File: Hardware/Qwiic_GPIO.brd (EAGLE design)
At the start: 38.1 x 38.1 mm, 65 parts, among them J2 SMD, J3 PTH, J4 SMD, U3 TCA9534U

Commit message: Panel/production files
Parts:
- moved U$33 1.65 mm to (5.21, 5.46)
- moved U$34 1.65 mm to (3.56, 5.46)
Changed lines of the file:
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@@
 <layer number="23" name="tOrigins" color="15" fill="1" visible="yes" active="yes"/>
 <layer number="24" name="bOrigins" color="15" fill="1" visible="yes" active="yes"/>
-<layer number="25" name="tNames" color="7" fill="1" visible="no" active="yes"/>
-<layer number="26" name="bNames" color="7" fill="1" visible="no" active="yes"/>
-<layer number="27" name="tValues" color="7" fill="1" visible="no" active="yes"/>
-<layer number="28" name="bValues" color="7" fill="1" visible="no" active="yes"/>
-<layer number="29" name="tStop" color="7" fill="3" visible="no" active="yes"/>
-<layer number="30" name="bStop" color="7" fill="6" visible="no" active="yes"/>
-<layer number="31" name="tCream" color="7" fill="4" visible="no" active="yes"/>
-<layer number="32" name="bCream" color="7" fill="5" visible="no" active="yes"/>
-<layer number="33" name="tFinish" color="6" fill="3" visible="no" active="yes"/>
-<layer number="34" name="bFinish" color="6" fill="6" visible="no" active="yes"/>
-<layer number="35" name="tGlue" color="7" fill="4" visible="no" active="yes"/>
-<layer number="36" name="bGlue" color="7" fill="5" visible="no" active="yes"/>
-<layer number="37" name="tTest" color="7" fill="1" visible="no" active="yes"/>
-<layer number="38" name="bTest" color="7" fill="1" visible="no" active="yes"/>
-<layer number="39" name="tKeepout" color="4" fill="11" visible="no" active="yes"/>
-<layer number="40" name="bKeepout" color="1" fill="11" visible="no" active="yes"/>
-<layer number="41" name="tRestrict" color="4" fill="10" visible="no" active="yes"/>
-<layer number="42" name="bRestrict" color="1" fill="10" visible="no" active="yes"/>
-<layer number="43" name="vRestrict" color="2" fill="10" visible="no" active="yes"/>
-<layer number="44" name="Drills" color="7" fill="1" visible="no" active="yes"/>
+<layer number="25" name="tNames" color="7" fill="1" visible="yes" active="yes"/>
+<layer number="26" name="bNames" color="7" fill="1" visible="yes" active="yes"/>
+<layer number="27" name="tValues" color="7" fill="1" visible="yes" active="yes"/>
+<layer number="28" name="bValues" color="7" fill="1" visible="yes" active="yes"/>
+<layer number="29" name="tStop" color="7" fill="3" visible="yes" active="yes"/>
+<layer number="30" name="bStop" color="7" fill="6" visible="yes" active="yes"/>
+<layer number="31" name="tCream" color="7" fill="4" visible="yes" active="yes"/>
+<layer number="32" name="bCream" color="7" fill="5" visible="yes" active="yes"/>
+<layer number="33" name="tFinish" color="6" fill="3" visible="yes" active="yes"/>
+<layer number="34" name="bFinish" color="6" fill="6" visible="yes" active="yes"/>
+<layer number="35" name="tGlue" color="7" fill="4" visible="yes" active="yes"/>
+<layer number="36" name="bGlue" color="7" fill="5" visible="yes" active="yes"/>
+<layer number="37" name="tTest" color="7" fill="1" visible="yes" active="yes"/>
+<layer number="38" name="bTest" color="7" fill="1" visible="yes" active="yes"/>
+<layer number="39" name="tKeepout" color="4" fill="11" visible="yes" active="yes"/>
+<layer number="40" name="bKeepout" color="1" fill="11" visible="yes" active="yes"/>
+<layer number="41" name="tRestrict" color="4" fill="10" visible="yes" active="yes"/>
+<layer number="42" name="bRestrict" color="1" fill="10" visible="yes" active="yes"/>
+<layer number="43" name="vRestrict" color="2" fill="10" visible="yes" active="yes"/>
+<layer number="44" name="Drills" color="7" fill="1" visible="yes" active="yes"/>
 <layer number="45" name="Holes" color="7" fill="1" visible="yes" active="yes"/>
-<layer number="46" name="Milling" color="3" fill="1" visible="no" active="yes"/>
-<layer number="47" name="Measures" color="7" fill="1" visible="no" active="yes"/>
-<layer number="48" name="Document" color="7" fill="1" visible="no" active="yes"/>
-<layer number="49" name="Reference" color="7" fill="1" visible="no" active="yes"/>
-<layer number="50" name="dxf" color="7" fill="1" visible="no" active="yes"/>
+<layer number="46" name="Milling" color="3" fill="1" visible="yes" active="yes"/>
+<layer number="47" name="Measures" color="7" fill="1" visible="yes" active="yes"/>
+<layer number="48" name="Document" color="7" fill="1" visible="yes" active="yes"/>
+<layer number="49" name="Reference" color="7" fill="1" visible="yes" active="yes"/>
+<layer number="50" name="dxf" color="7" fill="1" visible="yes" active="yes"/>
 <layer number="51" name="tDocu" color="6" fill="1" visible="yes" active="yes"/>
-<layer number="52" name="bDocu" color="7" fill="1" visible="no" active="yes"/>
+<layer number="52" name="bDocu" color="7" fill="1" visible="yes" active="yes"/>
 <layer number="91" name="Nets" color="2" fill="1" visible="no" active="no"/>
 <layer number="92" name="Busses" color="1" fill="1" visible="no" active="no"/>
@@
 <element name="U$37" library="buzzard_labels (5)" package="04" value="" x="3.683" y="29.845" smashed="yes" rot="R90"/>
 <element name="U$29" library="buzzard_labels (5)" package="15" value="" x="5.461" y="29.972" smashed="yes" rot="R90"/>
-<element name="U$33" library="buzzard_labels (5)" package="20" value="" x="3.556" y="5.461" smashed="yes" rot="R90"/>
-<element name="U$34" library="buzzard_labels (5)" package="31" value="" x="5.207" y="5.461" smashed="yes" rot="R90"/>
+<element name="U$33" library="buzzard_labels (5)" package="20" value="" x="5.207" y="5.461" smashed="yes" rot="R90"/>
+<element name="U$34" library="buzzard_labels (5)" package="31" value="" x="3.556" y="5.461" smashed="yes" rot="R90"/>
 <element name="U$35" library="buzzard_labels (5)" package="GND2" value="" x="1.905" y="28.829" smashed="yes" rot="R90"/>
 <element name="U$38" library="buzzard_labels (5)" package="3V33" value="" x="7.239" y="28.829" smashed="yes" rot="R90"/>

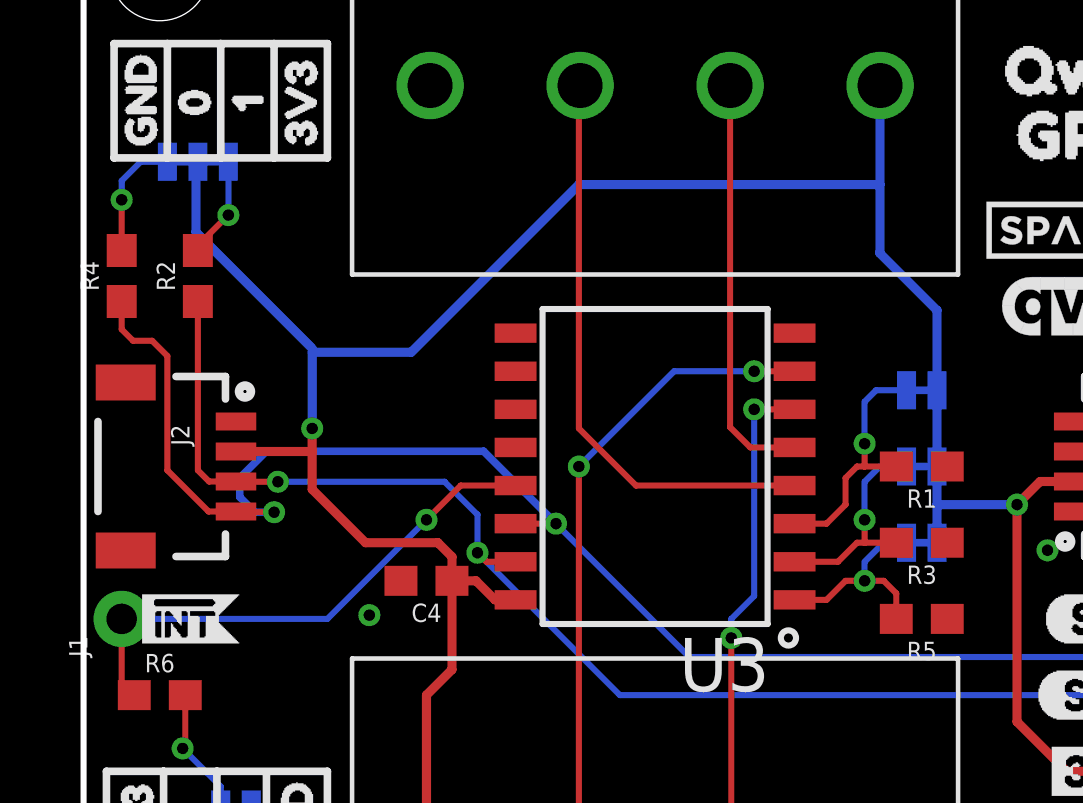
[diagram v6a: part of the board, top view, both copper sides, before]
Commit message: Added PWR LED, made labels larger
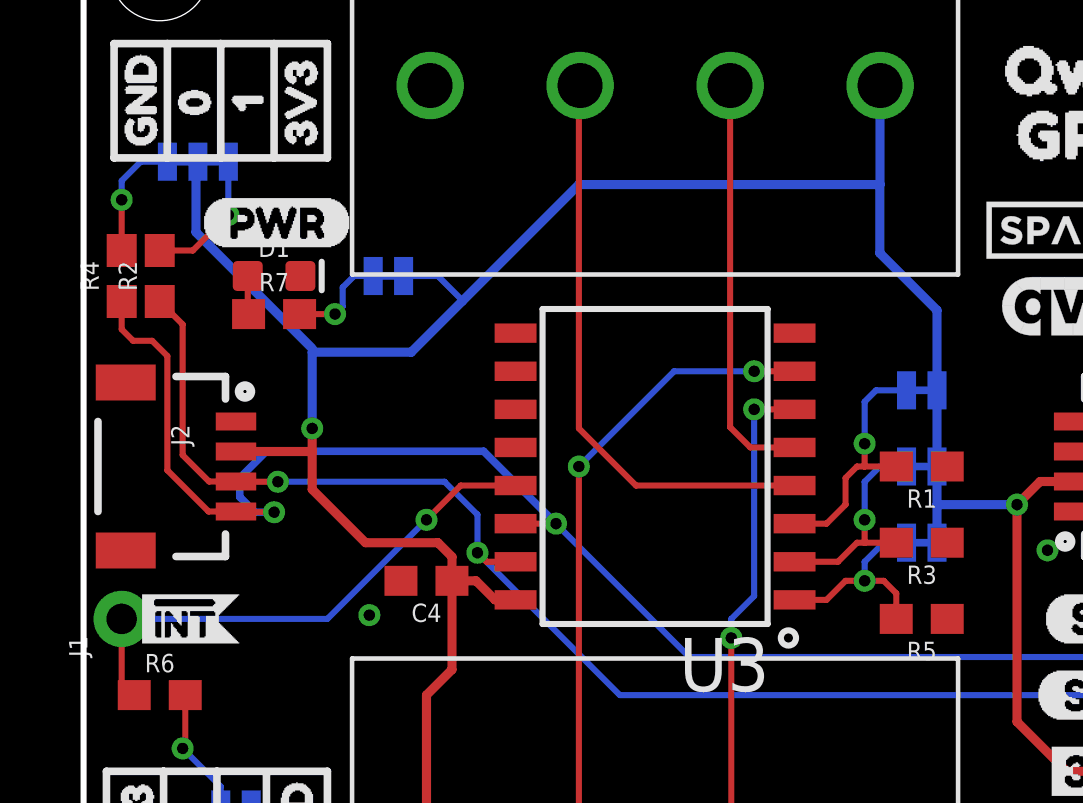
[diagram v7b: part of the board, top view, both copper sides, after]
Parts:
- removed U$14, U$15: (no value), buzzard_labels (47):__3V3__3
- removed U$16: (no value), buzzard_labels (49):_____1_____1
- removed U$17: (no value), buzzard_labels (49):______0______0
- removed U$18: (no value), buzzard_labels (48):_____3_____2
- removed U$19: (no value), buzzard_labels (48):______2______1
- removed U$4, U$6: (no value), buzzard_labels (48):__GND__0
- added 3V3: JUMPER-SMT_2_NC_TRACE_SILK, SparkFun-Jumpers:SMT-JUMPER_2_NC_TRACE_SILK
- added D1: RED, SparkFun-LED:LED-0603
- added R7: 1k, SparkFun-Resistors:0603
- added U$30, U$31: (no value), buzzard_labels (66):INT1
- added U$39, U$40: (no value), buzzard_labels (66):PWR0
- added U$41: (no value), buzzard_labels (68):____0____1
- added U$42: (no value), buzzard_labels (68):____2____3
- added U$43: (no value), buzzard_labels (68):____3____4
- added U$44: (no value), buzzard_labels (68):_____1____2
- added U$45, U$46: (no value), buzzard_labels (68):GND0
- added U$47, U$48: (no value), buzzard_labels (71):_3V3_0
- moved R2 1.27 mm to (2.54, 25.4)
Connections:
- new net N$2: D1.A, R7.1
- new net N$3: 3V3.1, R7.2
- net 3.3V: now also 3V3.2
- net GND: now also D1.C
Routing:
- net N$3: track 0.00 -> 3.35 mm, vias 0 -> 1
- net 3.3V: track 95.4 -> 97.8 mm
- net N$2: track 0.00 -> 1.28 mm
- net SCL_PU1: track 3.38 -> 4.55 mm
- net SDA: track 55.2 -> 55.7 mm
